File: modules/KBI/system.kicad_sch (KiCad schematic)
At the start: 10 parts, among them J1 +15V, J2 -15V, J3 GND, J4 KOV, J5 GATE, J6 FM

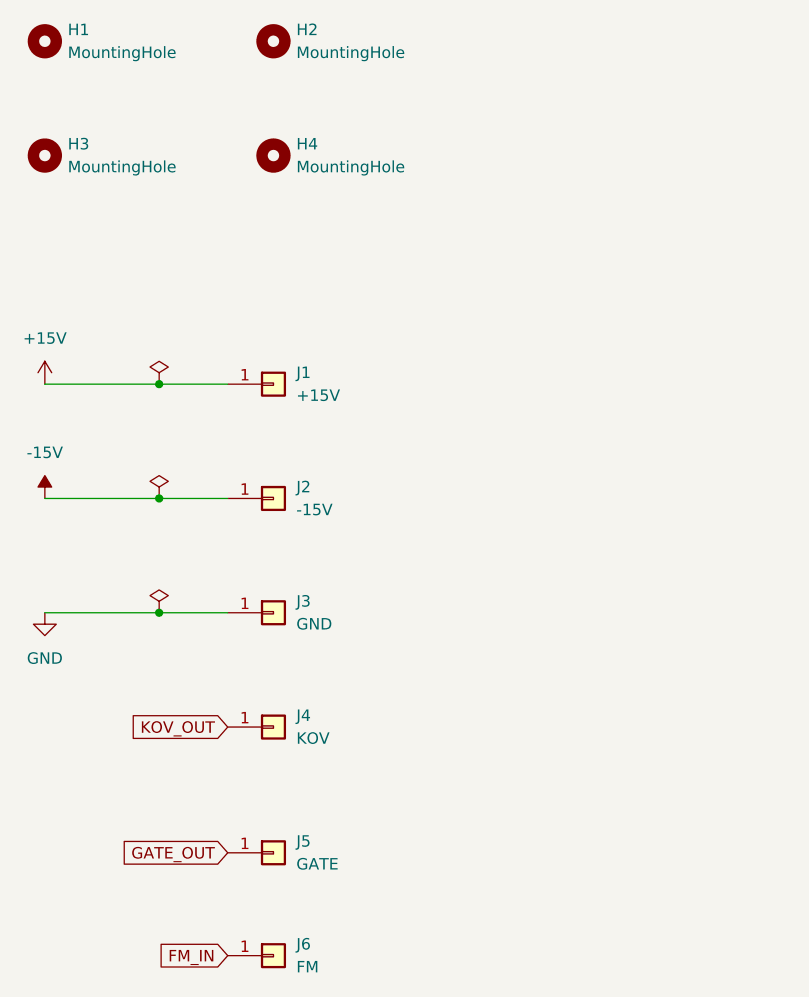
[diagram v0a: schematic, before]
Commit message: initialized 6U modules
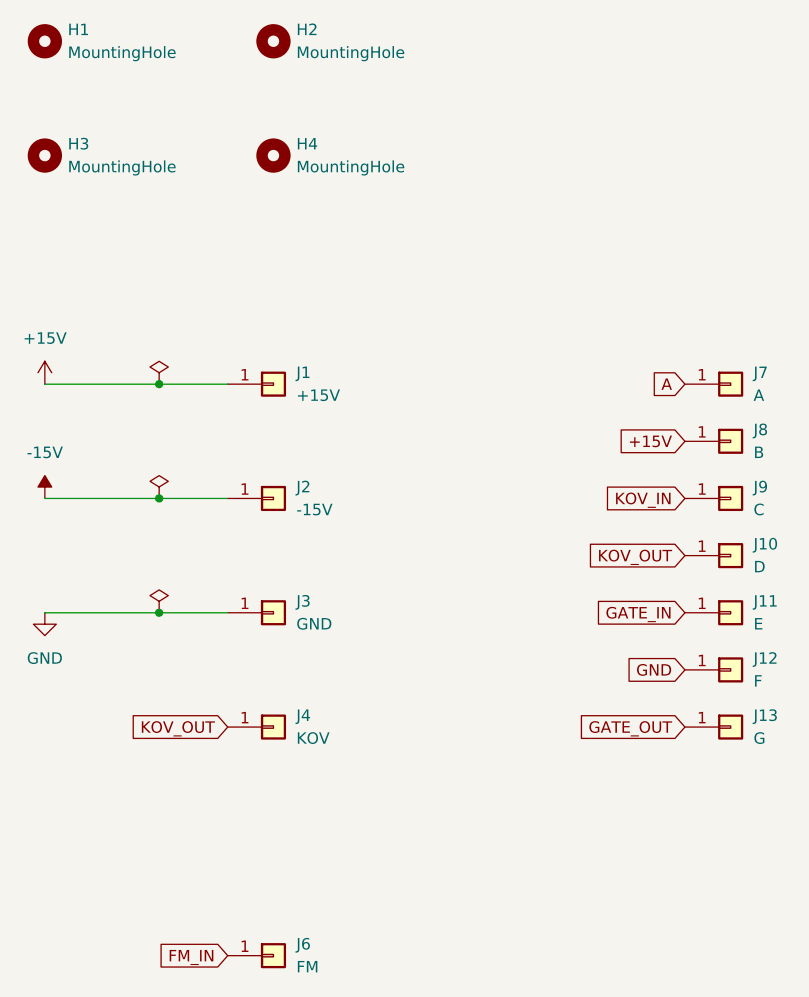
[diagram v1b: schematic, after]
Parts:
- removed J5: GATE, FormantKO:Wire_1x01_General, symbol FormantKO:Wire_1x01
- added J10: D, FormantKO:Wire_1x01_General, symbol FormantKO:Wire_1x01
- added J11: E, FormantKO:Wire_1x01_General, symbol FormantKO:Wire_1x01
- added J12: F, FormantKO:Wire_1x01_General, symbol FormantKO:Wire_1x01
- added J13: G, FormantKO:Wire_1x01_General, symbol FormantKO:Wire_1x01
- added J7: A, FormantKO:Wire_1x01_General, symbol FormantKO:Wire_1x01
- added J8: B, FormantKO:Wire_1x01_General, symbol FormantKO:Wire_1x01
- added J9: C, FormantKO:Wire_1x01_General, symbol FormantKO:Wire_1x01
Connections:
- net +15V: now also J8.1 (Pin_1)
- net GATE_OUT: now also J13.1 (Pin_1)
- net GND: now also J12.1 (Pin_1)
- net KOV_OUT: now also J10.1 (Pin_1)
- new net A: J7.1 (Pin_1)
- new net GATE_IN: J11.1 (Pin_1)
- new net KOV_IN: J9.1 (Pin_1)
